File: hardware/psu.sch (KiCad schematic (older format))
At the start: 14 parts

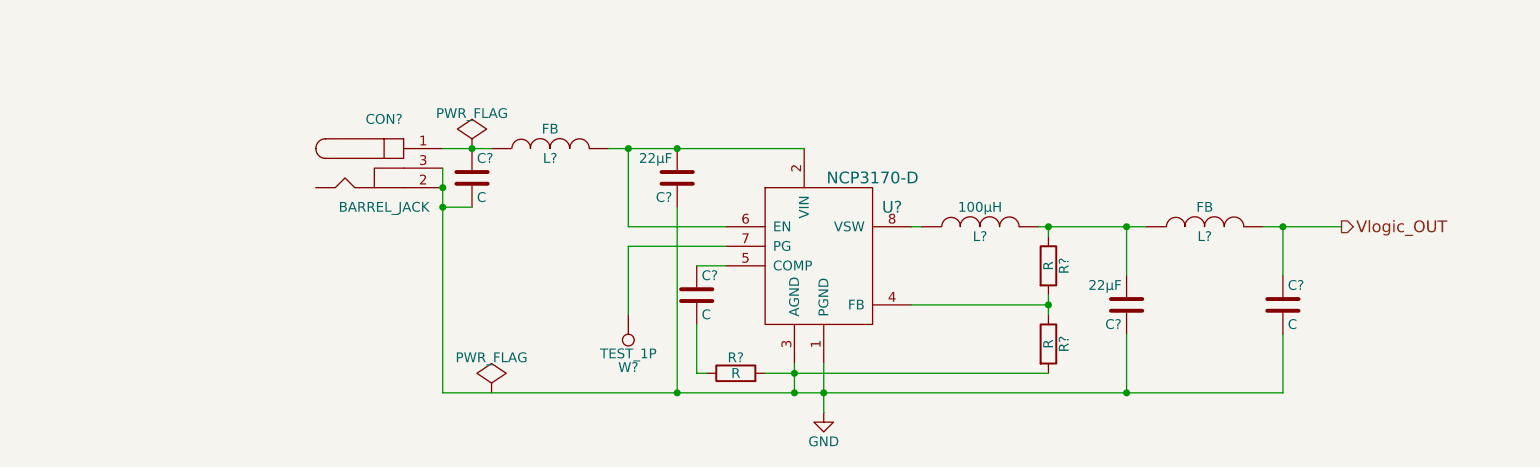
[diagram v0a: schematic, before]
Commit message: Added pull-up resistor for PG-pin in psu.sch
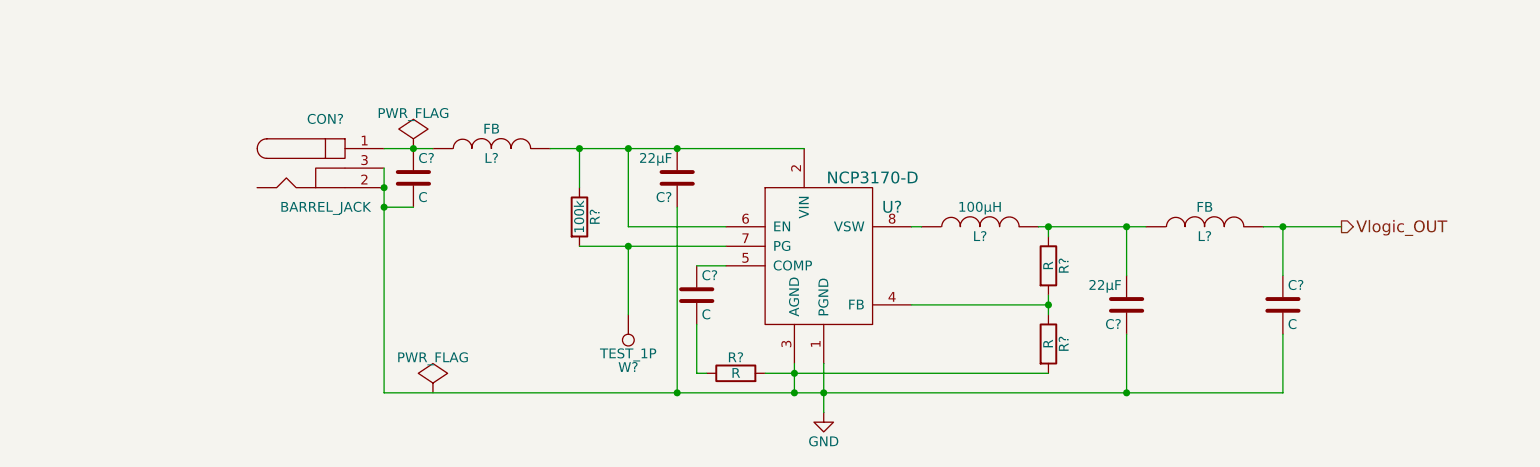
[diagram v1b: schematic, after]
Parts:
- added R?: 100k, symbol R
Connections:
- net at C?.2, L?.2, U?.2 (VIN)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: now also R?.1
- net at U?.7 (PG), W?.1: now also R?.2
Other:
- moved on the sheet: C?, CON?, L?
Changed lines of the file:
@@
 	5450 4050 5450 4300
 Wire Wire Line
-	3500 4200 7800 4200
+	3200 4200 7800 4200
 Wire Wire Line
-	7000 4200 7000 3900
+	7000 3900 7000 4200
 Wire Wire Line
 	7000 3350 7000 3600
 Connection ~ 6600 3350
-Wire Wire Line
-	5150 4100 6600 4100
 Wire Wire Line
 	5300 4050 5300 4200
@@
 L BARREL_JACK CON?
 U 1 1 57E323EC
-P 3200 3050
-F 0 "CON?" H 3200 3300 50  0000 C CNN
-F 1 "BARREL_JACK" H 3200 2850 50  0000 C CNN
-F 2 "" H 3200 3050 50  0000 C CNN
-F 3 "" H 3200 3050 50  0000 C CNN
-	1    3200 3050
+P 2900 3050
+F 0 "CON?" H 2900 3300 50  0000 C CNN
+F 1 "BARREL_JACK" H 2900 2850 50  0000 C CNN
+F 2 "" H 2900 3050 50  0000 C CNN
+F 3 "" H 2900 3050 50  0000 C CNN
+	1    2900 3050
 	1    0    0    -1
 $EndComp
 Connection ~ 4450 2950
 Wire Wire Line
-	3500 3050 3500 4200
+	3200 3050 3200 4200
 Connection ~ 5300 4200
-Connection ~ 3500 3150
+Connection ~ 3200 3150
 Connection ~ 7000 3350
 $Comp
@@
 	4450 3800 4450 3450
 Wire Wire Line
-	4450 3450 4950 3450
+	4200 3450 4950 3450
 Wire Wire Line
-	3500 2950 3750 2950
+	3200 2950 3450 2950
 $Comp
 L C C?
 U 1 1 57E32ACD
-P 3650 3100
-F 0 "C?" H 3675 3200 50  0000 L CNN
-F 1 "C" H 3675 3000 50  0000 L CNN
-F 2 "" H 3688 2950 50  0000 C CNN
-F 3 "" H 3650 3100 50  0000 C CNN
-	1    3650 3100
+P 3350 3100
+F 0 "C?" H 3375 3200 50  0000 L CNN
+F 1 "C" H 3375 3000 50  0000 L CNN
+F 2 "" H 3388 2950 50  0000 C CNN
+F 3 "" H 3350 3100 50  0000 C CNN
+	1    3350 3100
 	1    0    0    -1
 $EndComp
 Wire Wire Line
-	3650 3250 3500 3250
-Connection ~ 3500 3250
+	3350 3250 3200 3250
+Connection ~ 3200 3250
 $Comp
 L INDUCTOR L?
 U 1 1 57E32B5E
-P 4050 2950
-F 0 "L?" V 4000 2950 50  0000 C CNN
-F 1 "FB" V 4150 2950 50  0000 C CNN
-F 2 "" H 4050 2950 50  0000 C CNN
-F 3 "" H 4050 2950 50  0000 C CNN
-	1    4050 2950
+P 3750 2950
+F 0 "L?" V 3700 2950 50  0000 C CNN
+F 1 "FB" V 3850 2950 50  0000 C CNN
+F 2 "" H 3750 2950 50  0000 C CNN
+F 3 "" H 3750 2950 50  0000 C CNN
+	1    3750 2950
 	0    -1   -1   0
 $EndComp
-Connection ~ 3650 2950
+Connection ~ 3350 2950
 Wire Wire Line
-	4350 2950 5350 2950
+	4050 2950 5350 2950
 Wire Wire Line
 	4700 3250 4700 4200
@@
 L PWR_FLAG #FLG?
 U 1 1 57E334E3
-P 3650 2950
-F 0 "#FLG?" H 3650 3045 50  0001 C CNN
-F 1 "PWR_FLAG" H 3650 3130 50  0000 C CNN
-F 2 "" H 3650 2950 50  0000 C CNN
-F 3 "" H 3650 2950 50  0000 C CNN
-	1    3650 2950
+P 3350 2950
+F 0 "#FLG?" H 3350 3045 50  0001 C CNN
+F 1 "PWR_FLAG" H 3350 3130 50  0000 C CNN
+F 2 "" H 3350 2950 50  0000 C CNN
+F 3 "" H 3350 2950 50  0000 C CNN
+	1    3350 2950
 	1    0    0    -1
 $EndComp
@@
 L PWR_FLAG #FLG?
 U 1 1 57E33511
-P 3750 4200
-F 0 "#FLG?" H 3750 4295 50  0001 C CNN
-F 1 "PWR_FLAG" H 3750 4380 50  0000 C CNN
-F 2 "" H 3750 4200 50  0000 C CNN
-F 3 "" H 3750 4200 50  0000 C CNN
-	1    3750 4200
+P 3450 4200
+F 0 "#FLG?" H 3450 4295 50  0001 C CNN
+F 1 "PWR_FLAG" H 3450 4380 50  0000 C CNN
+F 2 "" H 3450 4200 50  0000 C CNN
+F 3 "" H 3450 4200 50  0000 C CNN
+	1    3450 4200
 	1    0    0    -1
 $EndComp
+Wire Wire Line
+	5150 4100 6600 4100
+$Comp
+L R R?
+U 1 1 57E40BA6
+P 4200 3300
+F 0 "R?" V 4280 3300 50  0000 C CNN
+F 1 "100k" V 4200 3300 50  0000 C CNN
+F 2 "" V 4130 3300 50  0000 C CNN
+F 3 "" H 4200 3300 50  0000 C CNN
+	1    4200 3300
+	1    0    0    -1
+$EndComp
+Wire Wire Line
+	4200 2950 4200 3150
+Connection ~ 4200 2950
+Connection ~ 4450 3450
 $EndSCHEMATC

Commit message: added rx/tx wm8731 (adc/dac)
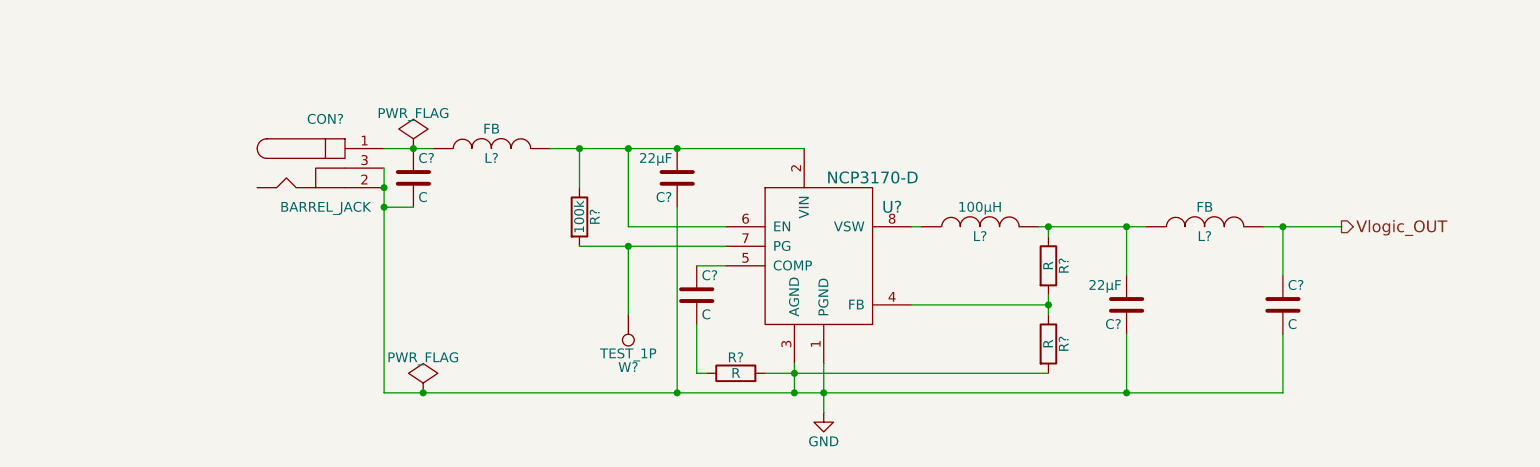
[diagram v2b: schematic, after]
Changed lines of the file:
@@
 	6600 3400 6600 3350
 Wire Wire Line
-	6550 3350 7100 3350
-Wire Wire Line
-	6600 3700 6600 3800
+	6550 3350 6600 3350
+Wire Wire Line
+	6600 3350 7000 3350
+Wire Wire Line
+	7000 3350 7100 3350
+Wire Wire Line
+	6600 3700 6600 3750
+Wire Wire Line
+	6600 3750 6600 3800
 Wire Wire Line
 	5900 3750 6600 3750
 Connection ~ 6600 3750
 Wire Wire Line
-	5450 4050 5450 4300
-Wire Wire Line
-	3200 4200 7800 4200
+	5450 4050 5450 4200
+Wire Wire Line
+	5450 4200 5450 4300
+Wire Wire Line
+	3200 4200 3400 4200
+Wire Wire Line
+	3400 4200 4700 4200
+Wire Wire Line
+	4700 4200 5300 4200
+Wire Wire Line
+	5300 4200 5450 4200
+Wire Wire Line
+	5450 4200 7000 4200
+Wire Wire Line
+	7000 4200 7800 4200
 Wire Wire Line
 	7000 3900 7000 4200
@@
 Connection ~ 6600 3350
 Wire Wire Line
-	5300 4050 5300 4200
+	5300 4050 5300 4100
+Wire Wire Line
+	5300 4100 5300 4200
 Wire Wire Line
 	4950 3350 4450 3350
@@
 Connection ~ 4450 2950
 Wire Wire Line
-	3200 3050 3200 4200
+	3200 3050 3200 3150
+Wire Wire Line
+	3200 3150 3200 3250
+Wire Wire Line
+	3200 3250 3200 4200
 Connection ~ 5300 4200
 Connection ~ 3200 3150
@@
 	4450 3800 4450 3450
 Wire Wire Line
-	4200 3450 4950 3450
-Wire Wire Line
-	3200 2950 3450 2950
+	4200 3450 4450 3450
+Wire Wire Line
+	4450 3450 4950 3450
+Wire Wire Line
+	3200 2950 3350 2950
+Wire Wire Line
+	3350 2950 3450 2950
 $Comp
 L C C?
@@
 Connection ~ 3350 2950
 Wire Wire Line
-	4050 2950 5350 2950
+	4050 2950 4200 2950
+Wire Wire Line
+	4200 2950 4450 2950
+Wire Wire Line
+	4450 2950 4700 2950
+Wire Wire Line
+	4700 2950 5350 2950
 Wire Wire Line
 	4700 3250 4700 4200
@@
 $EndComp
 Wire Wire Line
-	7700 3350 8100 3350
+	7700 3350 7800 3350
+Wire Wire Line
+	7800 3350 8100 3350
 Connection ~ 7800 3350
 Wire Wire Line
@@
 L PWR_FLAG #FLG?
 U 1 1 57E33511
-P 3450 4200
-F 0 "#FLG?" H 3450 4295 50  0001 C CNN
-F 1 "PWR_FLAG" H 3450 4380 50  0000 C CNN
-F 2 "" H 3450 4200 50  0000 C CNN
-F 3 "" H 3450 4200 50  0000 C CNN
-	1    3450 4200
-	1    0    0    -1
-$EndComp
-Wire Wire Line
-	5150 4100 6600 4100
+P 3400 4200
+F 0 "#FLG?" H 3400 4295 50  0001 C CNN
+F 1 "PWR_FLAG" H 3400 4380 50  0000 C CNN
+F 2 "" H 3400 4200 50  0000 C CNN
+F 3 "" H 3400 4200 50  0000 C CNN
+	1    3400 4200
+	1    0    0    -1
+$EndComp
+Wire Wire Line
+	5150 4100 5300 4100
+Wire Wire Line
+	5300 4100 6600 4100
 $Comp
 L R R?
@@
 Connection ~ 4200 2950
 Connection ~ 4450 3450
+Connection ~ 3400 4200
 $EndSCHEMATC

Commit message: Added TX chain schematic block and Vin netlist for input power_flag
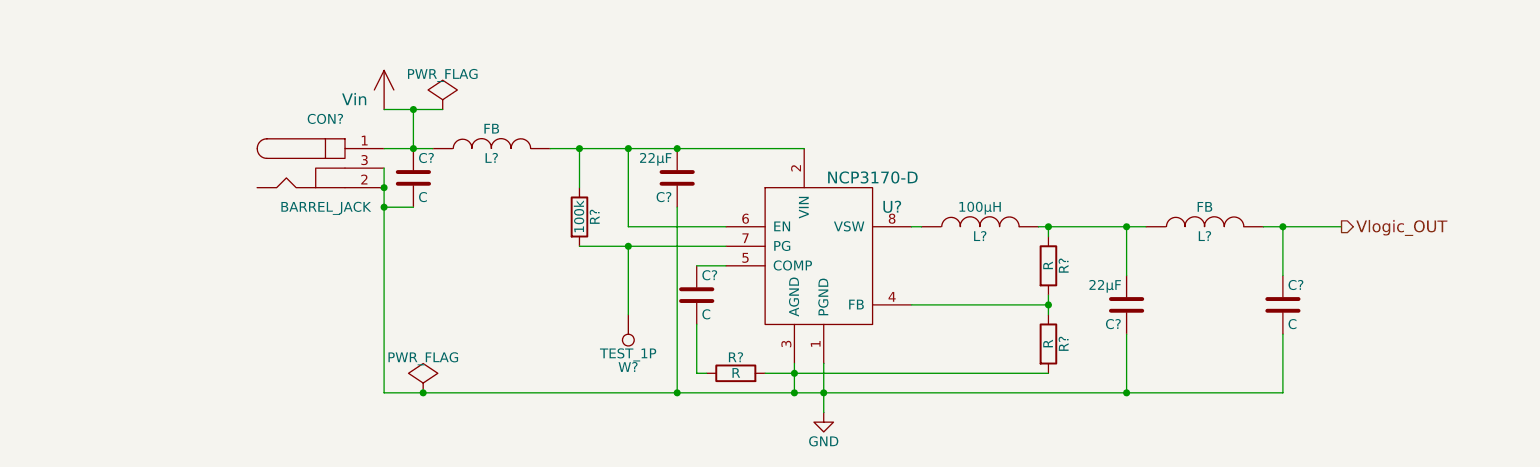
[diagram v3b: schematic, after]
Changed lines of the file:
@@
 $Descr A4 11693 8268
 encoding utf-8
-Sheet 4 4
+Sheet 4 5
 Title "Power supply unit"
 Date "2016-09-22"
@@
 	6600 3400 6600 3350
 Wire Wire Line
-	6550 3350 6600 3350
-Wire Wire Line
-	6600 3350 7000 3350
-Wire Wire Line
-	7000 3350 7100 3350
-Wire Wire Line
-	6600 3700 6600 3750
-Wire Wire Line
-	6600 3750 6600 3800
+	6550 3350 7100 3350
+Wire Wire Line
+	6600 3700 6600 3800
 Wire Wire Line
 	5900 3750 6600 3750
 Connection ~ 6600 3750
 Wire Wire Line
-	5450 4050 5450 4200
-Wire Wire Line
-	5450 4200 5450 4300
-Wire Wire Line
-	3200 4200 3400 4200
-Wire Wire Line
-	3400 4200 4700 4200
-Wire Wire Line
-	4700 4200 5300 4200
-Wire Wire Line
-	5300 4200 5450 4200
-Wire Wire Line
-	5450 4200 7000 4200
-Wire Wire Line
-	7000 4200 7800 4200
+	5450 4050 5450 4300
+Wire Wire Line
+	3200 4200 7800 4200
 Wire Wire Line
 	7000 3900 7000 4200
@@
 Connection ~ 6600 3350
 Wire Wire Line
-	5300 4050 5300 4100
-Wire Wire Line
-	5300 4100 5300 4200
+	5300 4050 5300 4200
 Wire Wire Line
 	4950 3350 4450 3350
@@
 Connection ~ 4450 2950
 Wire Wire Line
-	3200 3050 3200 3150
-Wire Wire Line
-	3200 3150 3200 3250
-Wire Wire Line
-	3200 3250 3200 4200
+	3200 3050 3200 4200
 Connection ~ 5300 4200
 Connection ~ 3200 3150
@@
 	4450 3800 4450 3450
 Wire Wire Line
-	4200 3450 4450 3450
-Wire Wire Line
-	4450 3450 4950 3450
-Wire Wire Line
-	3200 2950 3350 2950
-Wire Wire Line
-	3350 2950 3450 2950
+	4200 3450 4950 3450
+Wire Wire Line
+	3200 2950 3450 2950
 $Comp
 L C C?
@@
 	0    -1   -1   0
 $EndComp
-Connection ~ 3350 2950
-Wire Wire Line
-	4050 2950 4200 2950
-Wire Wire Line
-	4200 2950 4450 2950
-Wire Wire Line
-	4450 2950 4700 2950
-Wire Wire Line
-	4700 2950 5350 2950
+Wire Wire Line
+	4050 2950 5350 2950
 Wire Wire Line
 	4700 3250 4700 4200
@@
 $EndComp
 Wire Wire Line
-	7700 3350 7800 3350
-Wire Wire Line
-	7800 3350 8100 3350
+	7700 3350 8100 3350
 Connection ~ 7800 3350
 Wire Wire Line
@@
 Text HLabel 8100 3350 2    60   Output ~ 0
 Vlogic_OUT
-$Comp
-L PWR_FLAG #FLG?
-U 1 1 57E334E3
-P 3350 2950
-F 0 "#FLG?" H 3350 3045 50  0001 C CNN
-F 1 "PWR_FLAG" H 3350 3130 50  0000 C CNN
-F 2 "" H 3350 2950 50  0000 C CNN
-F 3 "" H 3350 2950 50  0000 C CNN
-	1    3350 2950
-	1    0    0    -1
-$EndComp
 $Comp
 L PWR_FLAG #FLG?
@@
 $EndComp
 Wire Wire Line
-	5150 4100 5300 4100
-Wire Wire Line
-	5300 4100 6600 4100
+	5150 4100 6600 4100
 $Comp
 L R R?
@@
 Connection ~ 4450 3450
 Connection ~ 3400 4200
+Connection ~ 3350 2950
+$Comp
+L PWR_FLAG #FLG?
+U 1 1 57E44620
+P 3500 2750
+F 0 "#FLG?" H 3500 2845 50  0001 C CNN
+F 1 "PWR_FLAG" H 3500 2930 50  0000 C CNN
+F 2 "" H 3500 2750 50  0000 C CNN
+F 3 "" H 3500 2750 50  0000 C CNN
+	1    3500 2750
+	1    0    0    -1
+$EndComp
+Wire Wire Line
+	3200 2750 3500 2750
+Wire Wire Line
+	3350 2750 3350 2950
+Connection ~ 3350 2750
+$Comp
+L Vin #Vin?
+U 1 1 57E44EE6
+P 3200 2750
+F 0 "#Vin?" H 3350 2800 60  0001 C CNN
+F 1 "Vin" H 3050 2800 60  0000 C CNN
+F 2 "" H 3200 2750 60  0001 C CNN
+F 3 "" H 3200 2750 60  0001 C CNN
+	1    3200 2750
+	1    0    0    -1
+$EndComp
 $EndSCHEMATC

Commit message: Added RX chain. also modified and cleand up other schemas
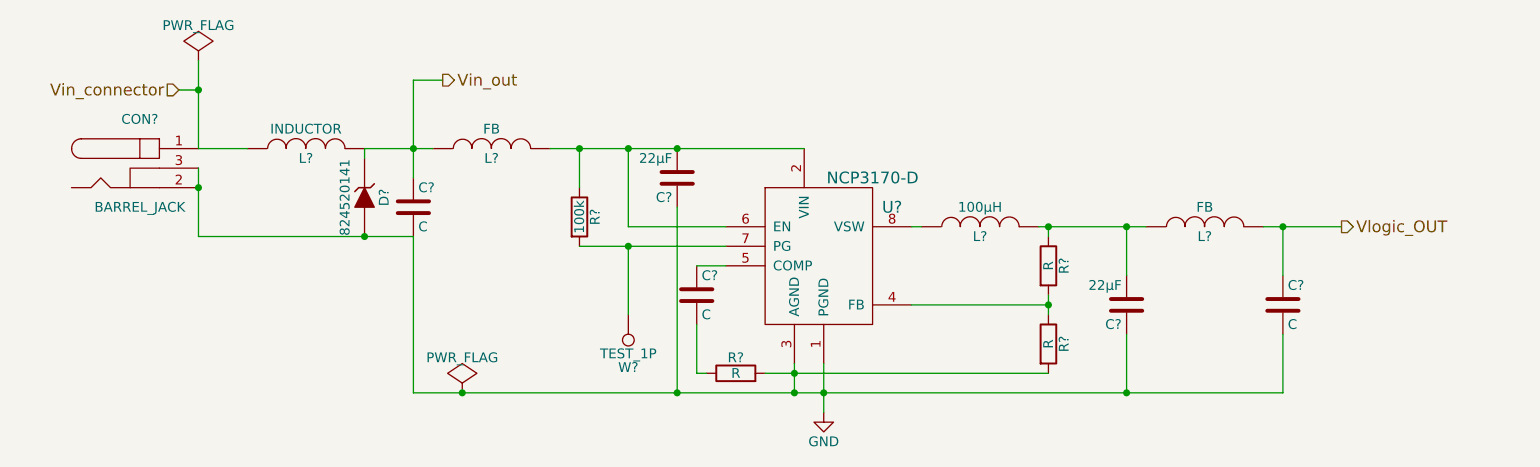
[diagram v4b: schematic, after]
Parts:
- added D?: 824520141, symbol ZENER
- added L?: INDUCTOR, symbol INDUCTOR
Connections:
- net GND: now also D?.2 (A)
- net Vin_out: now reaches C?.1, L?.1
- net Vin_out: now also D?.1 (K), L?.2; no longer CON?.1
- new net Vin_connector: CON?.1, L?.1
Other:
- moved on the sheet: C?, CON?
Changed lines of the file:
@@
 $Descr A4 11693 8268
 encoding utf-8
-Sheet 4 5
+Sheet 4 7
 Title "Power supply unit"
 Date "2016-09-22"
@@
 	5450 4050 5450 4300
 Wire Wire Line
-	3200 4200 7800 4200
+	3350 4200 7800 4200
 Wire Wire Line
 	7000 3900 7000 4200
@@
 Connection ~ 5450 4200
 $Comp
-L GND #PWR?
+L GND #PWR014
 U 1 1 57E32388
 P 5450 4300
-F 0 "#PWR?" H 5450 4050 50  0001 C CNN
+F 0 "#PWR014" H 5450 4050 50  0001 C CNN
 F 1 "GND" H 5450 4150 50  0000 C CNN
 F 2 "" H 5450 4300 50  0000 C CNN
@@
 L BARREL_JACK CON?
 U 1 1 57E323EC
-P 2900 3050
-F 0 "CON?" H 2900 3300 50  0000 C CNN
-F 1 "BARREL_JACK" H 2900 2850 50  0000 C CNN
-F 2 "" H 2900 3050 50  0000 C CNN
-F 3 "" H 2900 3050 50  0000 C CNN
-	1    2900 3050
+P 1950 3050
+F 0 "CON?" H 1950 3300 50  0000 C CNN
+F 1 "BARREL_JACK" H 1950 2850 50  0000 C CNN
+F 2 "" H 1950 3050 50  0000 C CNN
+F 3 "" H 1950 3050 50  0000 C CNN
+	1    1950 3050
 	1    0    0    -1
 $EndComp
 Connection ~ 4450 2950
 Wire Wire Line
-	3200 3050 3200 4200
+	2250 3050 2250 3400
 Connection ~ 5300 4200
-Connection ~ 3200 3150
+Connection ~ 2250 3150
 Connection ~ 7000 3350
 $Comp
@@
 Wire Wire Line
 	4200 3450 4950 3450
-Wire Wire Line
-	3200 2950 3450 2950
 $Comp
 L C C?
 U 1 1 57E32ACD
-P 3350 3100
-F 0 "C?" H 3375 3200 50  0000 L CNN
-F 1 "C" H 3375 3000 50  0000 L CNN
-F 2 "" H 3388 2950 50  0000 C CNN
-F 3 "" H 3350 3100 50  0000 C CNN
-	1    3350 3100
-	1    0    0    -1
-$EndComp
-Wire Wire Line
-	3350 3250 3200 3250
-Connection ~ 3200 3250
+P 3350 3250
+F 0 "C?" H 3375 3350 50  0000 L CNN
+F 1 "C" H 3375 3150 50  0000 L CNN
+F 2 "" H 3388 3100 50  0000 C CNN
+F 3 "" H 3350 3250 50  0000 C CNN
+	1    3350 3250
+	1    0    0    -1
+$EndComp
+Wire Wire Line
+	2250 3400 3350 3400
 $Comp
 L INDUCTOR L?
@@
 Vlogic_OUT
 $Comp
-L PWR_FLAG #FLG?
+L PWR_FLAG #FLG015
 U 1 1 57E33511
-P 3400 4200
-F 0 "#FLG?" H 3400 4295 50  0001 C CNN
-F 1 "PWR_FLAG" H 3400 4380 50  0000 C CNN
-F 2 "" H 3400 4200 50  0000 C CNN
-F 3 "" H 3400 4200 50  0000 C CNN
-	1    3400 4200
+P 3600 4200
+F 0 "#FLG015" H 3600 4295 50  0001 C CNN
+F 1 "PWR_FLAG" H 3600 4380 50  0000 C CNN
+F 2 "" H 3600 4200 50  0000 C CNN
+F 3 "" H 3600 4200 50  0000 C CNN
+	1    3600 4200
 	1    0    0    -1
 $EndComp
@@
 Connection ~ 4200 2950
 Connection ~ 4450 3450
-Connection ~ 3400 4200
+Connection ~ 3600 4200
 Connection ~ 3350 2950
 $Comp
-L PWR_FLAG #FLG?
+L PWR_FLAG #FLG016
 U 1 1 57E44620
-P 3500 2750
-F 0 "#FLG?" H 3500 2845 50  0001 C CNN
-F 1 "PWR_FLAG" H 3500 2930 50  0000 C CNN
-F 2 "" H 3500 2750 50  0000 C CNN
-F 3 "" H 3500 2750 50  0000 C CNN
-	1    3500 2750
-	1    0    0    -1
-$EndComp
-Wire Wire Line
-	3200 2750 3500 2750
-Wire Wire Line
-	3350 2750 3350 2950
-Connection ~ 3350 2750
-$Comp
-L Vin #Vin?
-U 1 1 57E44EE6
-P 3200 2750
-F 0 "#Vin?" H 3350 2800 60  0001 C CNN
-F 1 "Vin" H 3050 2800 60  0000 C CNN
-F 2 "" H 3200 2750 60  0001 C CNN
-F 3 "" H 3200 2750 60  0001 C CNN
-	1    3200 2750
-	1    0    0    -1
-$EndComp
+P 2250 2500
+F 0 "#FLG016" H 2250 2595 50  0001 C CNN
+F 1 "PWR_FLAG" H 2250 2680 50  0000 C CNN
+F 2 "" H 2250 2500 50  0000 C CNN
+F 3 "" H 2250 2500 50  0000 C CNN
+	1    2250 2500
+	1    0    0    -1
+$EndComp
+Text HLabel 2150 2650 0    60   Input ~ 0
+Vin_connector
+Wire Wire Line
+	2150 2650 2250 2650
+Wire Wire Line
+	2250 2500 2250 2950
+$Comp
+L INDUCTOR L?
+U 1 1 57E56F10
+P 2800 2950
+F 0 "L?" V 2750 2950 50  0000 C CNN
+F 1 "INDUCTOR" V 2900 2950 50  0000 C CNN
+F 2 "" H 2800 2950 50  0000 C CNN
+F 3 "" H 2800 2950 50  0000 C CNN
+	1    2800 2950
+	0    -1   -1   0
+$EndComp
+Wire Wire Line
+	3100 2950 3450 2950
+Connection ~ 2250 2650
+Wire Wire Line
+	3350 2600 3350 3100
+$Comp
+L ZENER D?
+U 1 1 57E57556
+P 3100 3200
+F 0 "D?" H 3100 3300 50  0000 C CNN
+F 1 "824520141" H 3100 3100 50  0000 C CNN
+F 2 "" H 3100 3200 50  0000 C CNN
+F 3 "" H 3100 3200 50  0000 C CNN
+	1    3100 3200
+	0    1    1    0
+$EndComp
+Connection ~ 3100 3400
+Wire Wire Line
+	3100 3000 3100 2950
+Wire Wire Line
+	2250 2950 2500 2950
+Wire Wire Line
+	3350 3400 3350 4200
+Text HLabel 3500 2600 2    60   Output ~ 0
+Vin_out
+Wire Wire Line
+	3500 2600 3350 2600
 $EndSCHEMATC
